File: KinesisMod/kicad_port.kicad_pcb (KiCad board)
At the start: 2 copper layers, 100 x 86 mm, 19 parts, among them J1 Conn_01x13, J2 Conn_01x13, J3 Conn_01x13, J4 Conn_01x13, J5 Conn_01x10, J6 Conn_01x10, M1 MountingHole_6.4mm_M6, M2 MountingHole_4.3mm_M4, M3 MountingHole_4.3mm_M4, M4 MountingHole_4.3mm_M4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

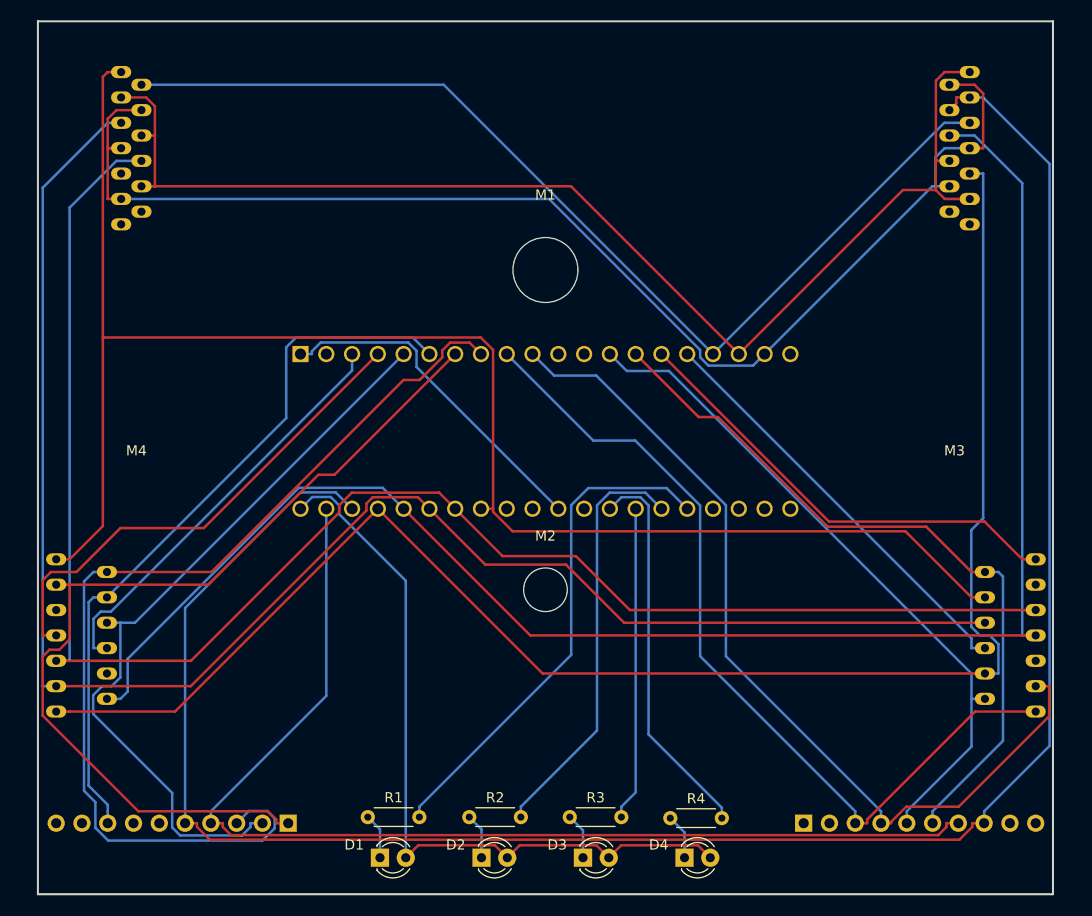
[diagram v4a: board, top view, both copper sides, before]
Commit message: add labels for LEDs
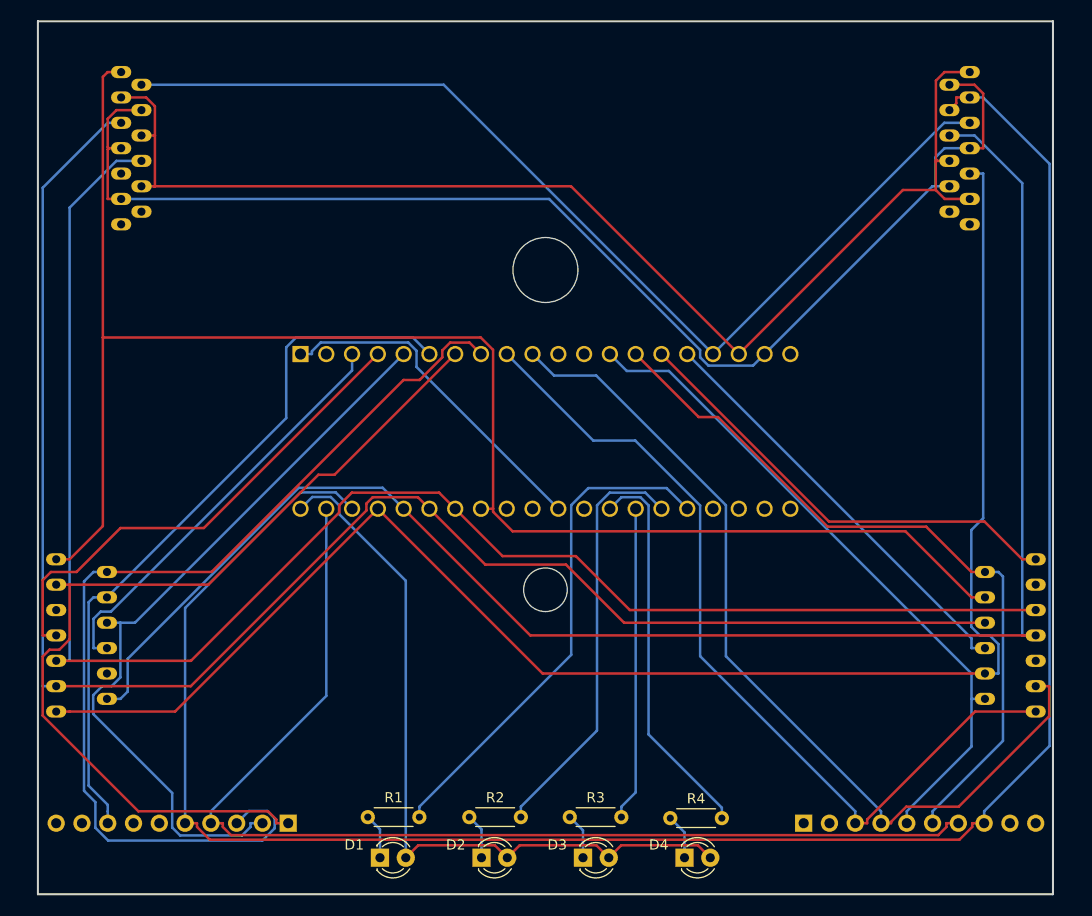
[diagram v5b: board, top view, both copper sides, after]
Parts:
- M1, M2, M3, M4: moved to B.Cu
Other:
- board text added: "CAPSLCK"
- board text added: "KEYPAD"
- board text added: "Kinesis Contoured 130 Teensy++ 2.0 QMK Firmware Mod Redesign by Aaron Silman Based off work by Michael Stapelberg"
- board text added: "NUMLCK"
- board text added: "SCRLCK"
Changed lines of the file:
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@@
   (general
     (thickness 1.6)
-    (drawings 22)
+    (drawings 27)
     (tracks 325)
     (zones 0)
@@
     )
   )
-  (module MountingHole:MountingHole_4.3mm_M4 (layer F.Cu)
+  (module MountingHole:MountingHole_4.3mm_M4 (layer B.Cu)
     (at 190.3 97.6)
     (descr "Mounting Hole 4.3mm, no annular, M4")
     (tags "mounting hole 4.3mm no annular m4")
     (attr virtual)
-    (fp_text reference M3 (at 0 -5.3) (layer F.SilkS)
-      (effects (font (size 1 1) (thickness 0.15)))
-    )
-    (fp_text value MountingHole_4.3mm_M4 (at 0 5.3) (layer F.Fab)
-      (effects (font (size 1 1) (thickness 0.15)))
-    )
-    (fp_circle (center 0 0) (end 4.55 0) (layer F.CrtYd) (width 0.05))
+    (fp_text reference M3 (at -0.2 -2.7) (layer B.SilkS)
+      (effects (font (size 1 1) (thickness 0.15)) (justify mirror))
+    )
+    (fp_text value MountingHole_4.3mm_M4 (at 0 -5.3) (layer B.Fab)
+      (effects (font (size 1 1) (thickness 0.15)) (justify mirror))
+    )
+    (fp_circle (center 0 0) (end 4.55 0) (layer B.CrtYd) (width 0.05))
     (fp_circle (center 0 0) (end 4.3 0) (layer Cmts.User) (width 0.15))
-    (fp_text user %R (at 0.3 0) (layer F.Fab)
-      (effects (font (size 1 1) (thickness 0.15)))
+    (fp_text user %R (at 0.3 0) (layer B.Fab)
+      (effects (font (size 1 1) (thickness 0.15)) (justify mirror))
     )
     (pad "" np_thru_hole oval (at 0 0) (size 4.6 2.25) (drill oval 4.6 2.25) (layers *.Cu *.Mask))
@@
     )
   )
-  (module MountingHole:MountingHole_4.3mm_M4 (layer F.Cu)
+  (module MountingHole:MountingHole_4.3mm_M4 (layer B.Cu)
     (at 109.7 97.6)
     (descr "Mounting Hole 4.3mm, no annular, M4")
     (tags "mounting hole 4.3mm no annular m4")
     (attr virtual)
-    (fp_text reference M4 (at 0 -5.3) (layer F.SilkS)
-      (effects (font (size 1 1) (thickness 0.15)))
-    )
-    (fp_text value MountingHole_4.3mm_M4 (at 0 5.3) (layer F.Fab)
-      (effects (font (size 1 1) (thickness 0.15)))
-    )
-    (fp_circle (center 0 0) (end 4.55 0) (layer F.CrtYd) (width 0.05))
+    (fp_text reference M4 (at 0 -3.2) (layer B.SilkS)
+      (effects (font (size 1 1) (thickness 0.15)) (justify mirror))
+    )
+    (fp_text value MountingHole_4.3mm_M4 (at 0 -5.3) (layer B.Fab)
+      (effects (font (size 1 1) (thickness 0.15)) (justify mirror))
+    )
+    (fp_circle (center 0 0) (end 4.55 0) (layer B.CrtYd) (width 0.05))
     (fp_circle (center 0 0) (end 4.3 0) (layer Cmts.User) (width 0.15))
-    (fp_text user %R (at 0.3 0) (layer F.Fab)
-      (effects (font (size 1 1) (thickness 0.15)))
+    (fp_text user %R (at 0.3 0) (layer B.Fab)
+      (effects (font (size 1 1) (thickness 0.15)) (justify mirror))
     )
     (pad "" np_thru_hole oval (at 0 0) (size 4.6 2.25) (drill oval 4.6 2.25) (layers *.Cu *.Mask))
@@
     )
   )
-  (module Mounting_Holes:MountingHole_4.3mm_M4 (layer F.Cu)
+  (module Mounting_Holes:MountingHole_4.3mm_M4 (layer B.Cu)
     (at 150 106)
     (descr "Mounting Hole 4.3mm, no annular, M4")
     (tags "mounting hole 4.3mm no annular m4")
-    (fp_text reference M2 (at 0 -5.3) (layer F.SilkS)
-      (effects (font (size 1 1) (thickness 0.15)))
-    )
-    (fp_text value MountingHole_4.3mm_M4 (at 0 5.3) (layer F.Fab)
-      (effects (font (size 1 1) (thickness 0.15)))
-    )
-    (fp_circle (center 0 0) (end 4.55 0) (layer F.CrtYd) (width 0.05))
+    (fp_text reference M2 (at 0 4.2) (layer B.SilkS)
+      (effects (font (size 1 1) (thickness 0.15)) (justify mirror))
+    )
+    (fp_text value MountingHole_4.3mm_M4 (at 0 -5.3) (layer B.Fab)
+      (effects (font (size 1 1) (thickness 0.15)) (justify mirror))
+    )
+    (fp_circle (center 0 0) (end 4.55 0) (layer B.CrtYd) (width 0.05))
     (fp_circle (center 0 0) (end 4.3 0) (layer Cmts.User) (width 0.15))
     (pad 1 np_thru_hole circle (at 0 0) (size 4.3 4.3) (drill 4.3) (layers *.Cu *.Mask))
   )
-  (module Mounting_Holes:MountingHole_6.4mm_M6 (layer F.Cu)
+  (module Mounting_Holes:MountingHole_6.4mm_M6 (layer B.Cu)
     (at 150 74.5)
     (descr "Mounting Hole 6.4mm, no annular, M6")
     (tags "mounting hole 6.4mm no annular m6")
-    (fp_text reference M1 (at 0 -7.4) (layer F.SilkS)
-      (effects (font (size 1 1) (thickness 0.15)))
-    )
-    (fp_text value MountingHole_6.4mm_M6 (at 0 7.4) (layer F.Fab)
-      (effects (font (size 1 1) (thickness 0.15)))
-    )
-    (fp_circle (center 0 0) (end 6.65 0) (layer F.CrtYd) (width 0.05))
+    (fp_text reference M1 (at -0.1 -5.4) (layer B.SilkS)
+      (effects (font (size 1 1) (thickness 0.15)) (justify mirror))
+    )
+    (fp_text value MountingHole_6.4mm_M6 (at 0 -7.4) (layer B.Fab)
+      (effects (font (size 1 1) (thickness 0.15)) (justify mirror))
+    )
+    (fp_circle (center 0 0) (end 6.65 0) (layer B.CrtYd) (width 0.05))
     (fp_circle (center 0 0) (end 6.4 0) (layer Cmts.User) (width 0.15))
     (pad 1 np_thru_hole circle (at 0 0) (size 6.4 6.4) (drill 6.4) (layers *.Cu *.Mask))
   )
+  (gr_text CAPSLCK (at 134.9 126.2) (layer B.SilkS)
+    (effects (font (size 1.5 1.5) (thickness 0.3)) (justify mirror))
+  )
+  (gr_text NUMLCK (at 145.3 126.1) (layer B.SilkS)
+    (effects (font (size 1.5 1.5) (thickness 0.3)) (justify mirror))
+  )
+  (gr_text SCRLCK (at 155.1 126) (layer B.SilkS)
+    (effects (font (size 1.5 1.5) (thickness 0.3)) (justify mirror))
+  )
+  (gr_text KEYPAD (at 164.8 125.9) (layer B.SilkS)
+    (effects (font (size 1.5 1.5) (thickness 0.3)) (justify mirror))
+  )
+  (gr_text "Kinesis Contoured 130\nTeensy++ 2.0 QMK Firmware Mod\nRedesign by Aaron Silman\nBased off work by Michael Stapelberg" (at 149.3 61.6) (layer B.SilkS)
+    (effects (font (size 1.5 1.5) (thickness 0.3)) (justify mirror))
+  )
   (dimension 7 (width 0.3) (layer Dwgs.User)

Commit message: add actual 10-pin header model and moved parts over so they arent hanging off board, re-routed
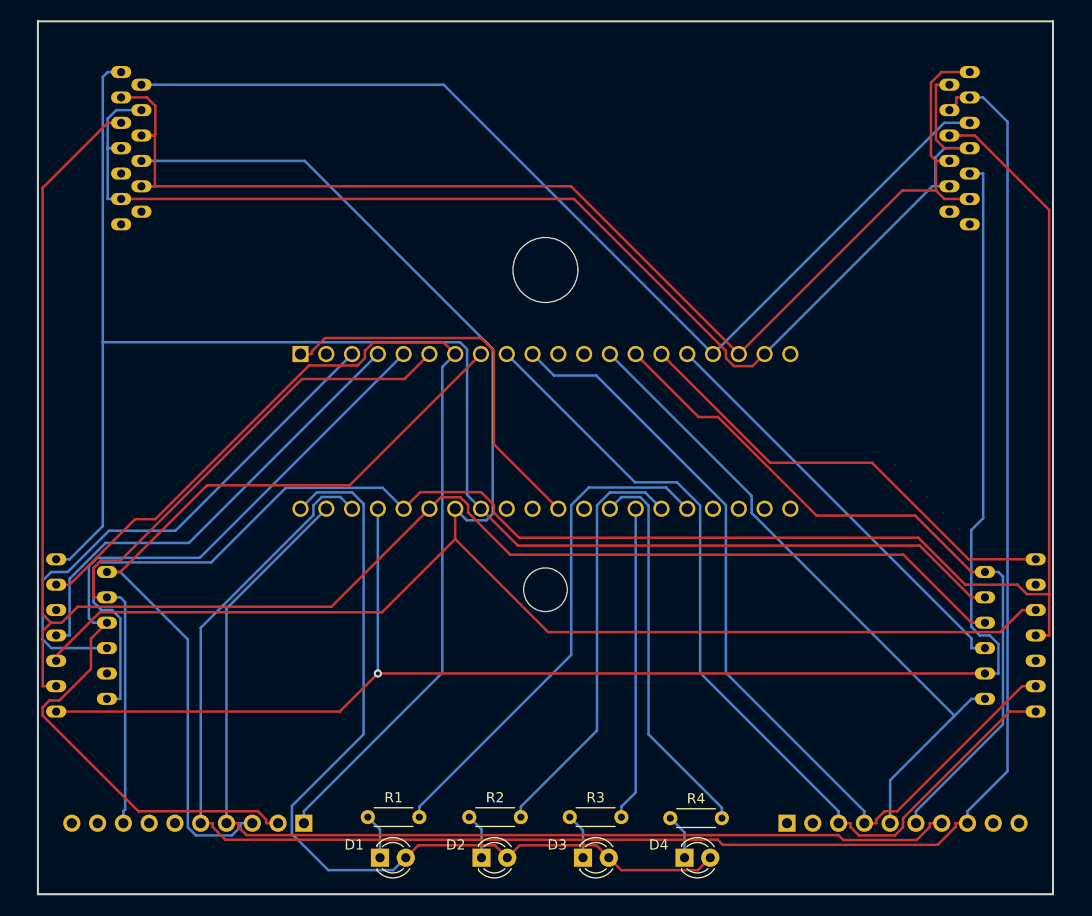
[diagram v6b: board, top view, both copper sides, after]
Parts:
- moved J5 1.64 mm to (173.8, 129.0)
- moved J6 1.54 mm to (126.2, 129.0)
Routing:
- net /PD5: track 98.7 -> 82.4 mm
- net +5V: track 75.1 -> 89.0 mm
- net /PB3: track 163.0 -> 175.6 mm
- net /PD2: track 75.2 -> 86.9 mm
- net /PD0: track 41.4 -> 52.2 mm
- net /PD4: track 92.1 -> 102.5 mm
- net /PB1: track 163.5 -> 172.4 mm
- net /PB5: track 204.6 -> 196.6 mm
- net GND: track 33.8 -> 38.6 mm
- net /PB6: track 110.7 -> 107.3 mm
- net /PD7: track 88.2 -> 84.9 mm
- net /PB4: track 160.6 -> 163.3 mm, vias 0 -> 1
- net /PD1: track 49.0 -> 46.4 mm
- net /PD6: track 85.4 -> 87.9 mm
- net /PB0: track 160.2 -> 157.9 mm
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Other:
- board text added: "Kinesis Contoured 130 Teensy++ 2.0 QMK Firmware Mod V1.0 RevA Redesign by Aaron Silman 2019-02 Based on work by Michael Stapelberg"
- board text removed: "Kinesis Contoured 130 Teensy++ 2.0 QMK Firmware Mod Redesign by Aaron Silman Based off work by Michael Stapelberg"

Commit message: slight board edit and double checking all pins. Should be good to send to fab after adding more Silk
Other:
- board text added: "Kinesis Contoured/Advantage Teensy++ 2.0 QMK Firmware Mod V1.0 RevA Redesign by Aaron Silman 2019-02 Based on work by Michael Stapelberg"
- board text removed: "Kinesis Contoured 130 Teensy++ 2.0 QMK Firmware Mod V1.0 RevA Redesign by Aaron Silman 2019-02 Based on work by Michael Stapelberg"
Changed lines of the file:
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@@
       (effects (font (size 1 1) (thickness 0.15)) (justify mirror))
     )
-    (fp_text user %R (at 0 2.33 270) (layer B.Fab)
+    (fp_text user %R (at -3.9 -0.1 270) (layer B.SilkS)
       (effects (font (size 1 1) (thickness 0.15)) (justify mirror))
     )
@@
     (descr "Through hole straight pin header, 1x10, 2.54mm pitch, single row")
     (tags "Through hole pin header THT 1x10 2.54mm single row")
-    (fp_text reference J6 (at 0 2.33 90) (layer B.SilkS)
+    (fp_text reference J6 (at 3.8 0.2 90) (layer B.SilkS)
       (effects (font (size 1 1) (thickness 0.15)) (justify mirror))
     )
@@
     (effects (font (size 1.5 1.5) (thickness 0.3)) (justify mirror))
   )
-  (gr_text "Kinesis Contoured 130\nTeensy++ 2.0 QMK Firmware Mod V1.0 RevA\nRedesign by Aaron Silman 2019-02\nBased on work by Michael Stapelberg" (at 149.3 61.6) (layer B.SilkS)
+  (gr_text "Kinesis Contoured/Advantage\nTeensy++ 2.0 QMK Firmware Mod V1.0 RevA\nRedesign by Aaron Silman 2019-02\nBased on work by Michael Stapelberg" (at 149.3 61.6) (layer B.SilkS)
     (effects (font (size 1.5 1.5) (thickness 0.3)) (justify mirror))
   )
@@
   )
   (dimension 80.600062 (width 0.3) (layer Dwgs.User)
-    (gr_text "80.600 mm" (at 149.953971 60.250029 0.0710865386) (layer Dwgs.User)
+    (gr_text "80.600 mm" (at 149.990199 89.450006 0.0710865386) (layer Dwgs.User)
       (effects (font (size 1.5 1.5) (thickness 0.3)))
     )
-    (feature1 (pts (xy 190.3 97.3) (xy 190.255848 61.713607)))
-    (feature2 (pts (xy 109.7 97.4) (xy 109.655848 61.813607)))
-    (crossbar (pts (xy 109.656576 62.400027) (xy 190.256576 62.300027)))
-    (arrow1a (pts (xy 190.256576 62.300027) (xy 189.130801 62.887845)))
-    (arrow1b (pts (xy 190.256576 62.300027) (xy 189.129346 61.715004)))
-    (arrow2a (pts (xy 109.656576 62.400027) (xy 110.783806 62.98505)))
-    (arrow2b (pts (xy 109.656576 62.400027) (xy 110.782351 61.812209)))
+    (feature1 (pts (xy 190.3 97.3) (xy 190.292076 90.913584)))
+    (feature2 (pts (xy 109.7 97.4) (xy 109.692076 91.013584)))
+    (crossbar (pts (xy 109.692804 91.600004) (xy 190.292804 91.500004)))
+    (arrow1a (pts (xy 190.292804 91.500004) (xy 189.167029 92.087822)))
+    (arrow1b (pts (xy 190.292804 91.500004) (xy 189.165574 90.914981)))
+    (arrow2a (pts (xy 109.692804 91.600004) (xy 110.820034 92.185027)))
+    (arrow2b (pts (xy 109.692804 91.600004) (xy 110.818579 91.012186)))
   )
   (dimension 9.7 (width 0.3) (layer Dwgs.User)

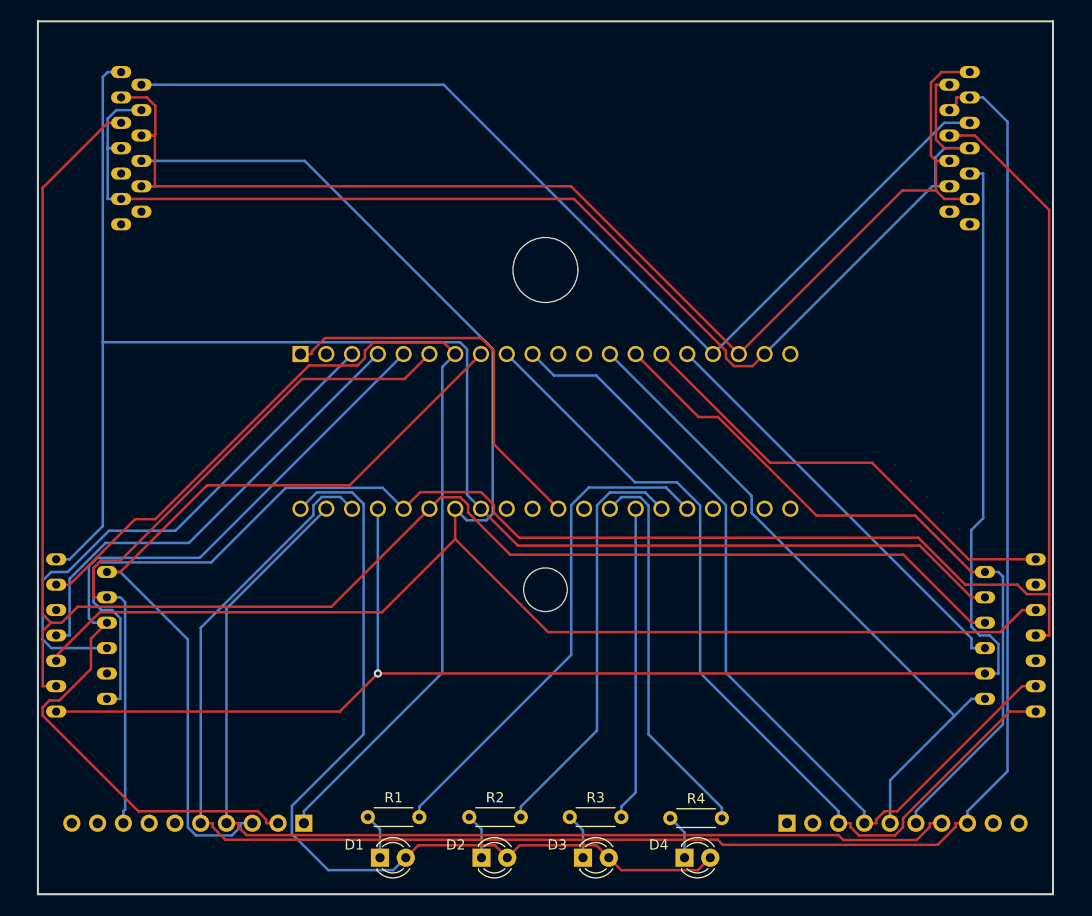
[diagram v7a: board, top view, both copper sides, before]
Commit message: re-placed F-row connectors closer to edge, re-routed
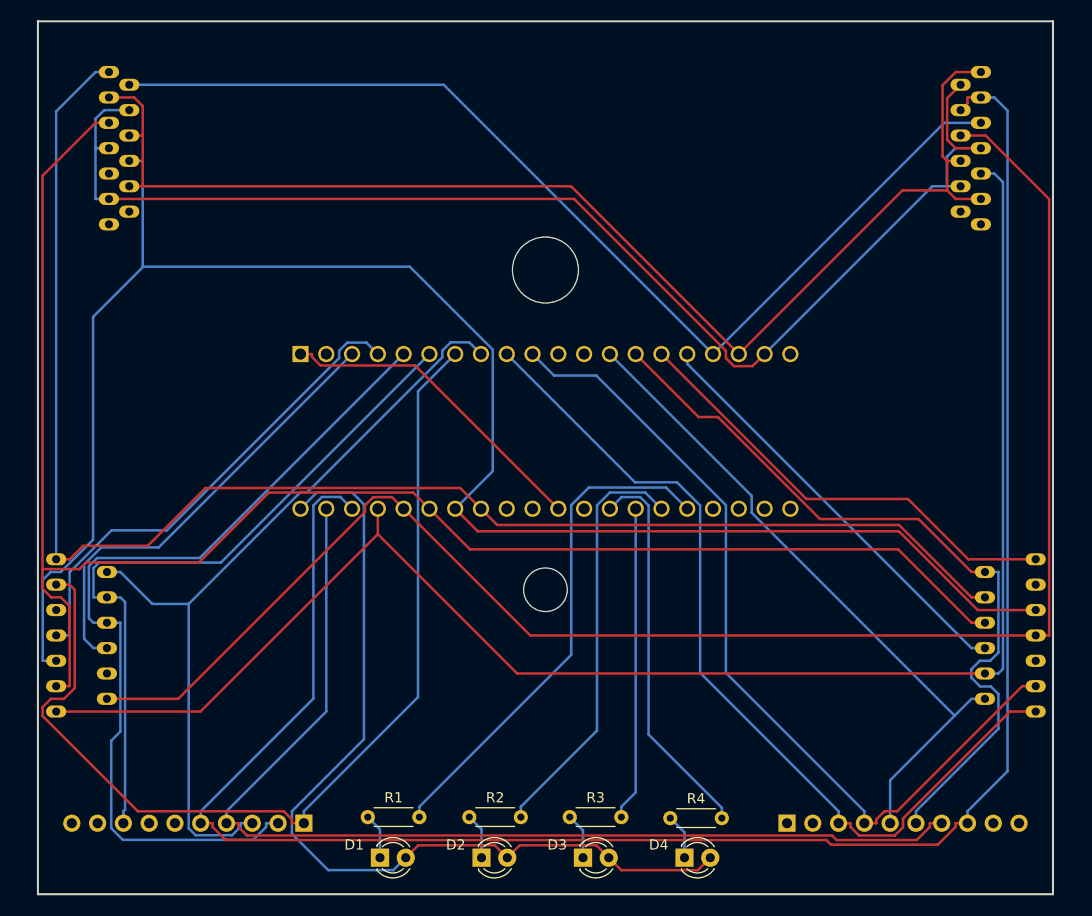
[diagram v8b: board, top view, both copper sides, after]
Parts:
- moved J2 1.20 mm to (108.0, 62.5)
- moved J1 1.10 mm to (191.9, 62.5)
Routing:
- net /PB3: track 175.6 -> 161.4 mm
- net /PB0: track 157.9 -> 149.8 mm
- net /PD0: track 52.2 -> 44.9 mm
- net GND: track 38.6 -> 31.9 mm
- net /PB4: track 163.3 -> 159.4 mm, vias 1 -> 0
- net /PD5: track 82.4 -> 79.1 mm
- net /PD4: track 102.5 -> 99.3 mm
- net /PC1: track 73.1 -> 76.2 mm
- net /PC4: track 102.0 -> 104.3 mm
- net /PC5: track 124.9 -> 126.9 mm
- net /PD1: track 46.4 -> 48.2 mm
- net /PC6: track 127.4 -> 128.9 mm
- net /PB2: track 164.2 -> 163.3 mm
- net /PB1: track 172.4 -> 173.0 mm
